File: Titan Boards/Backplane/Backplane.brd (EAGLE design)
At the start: 209.6 x 76.2 mm, 20 parts

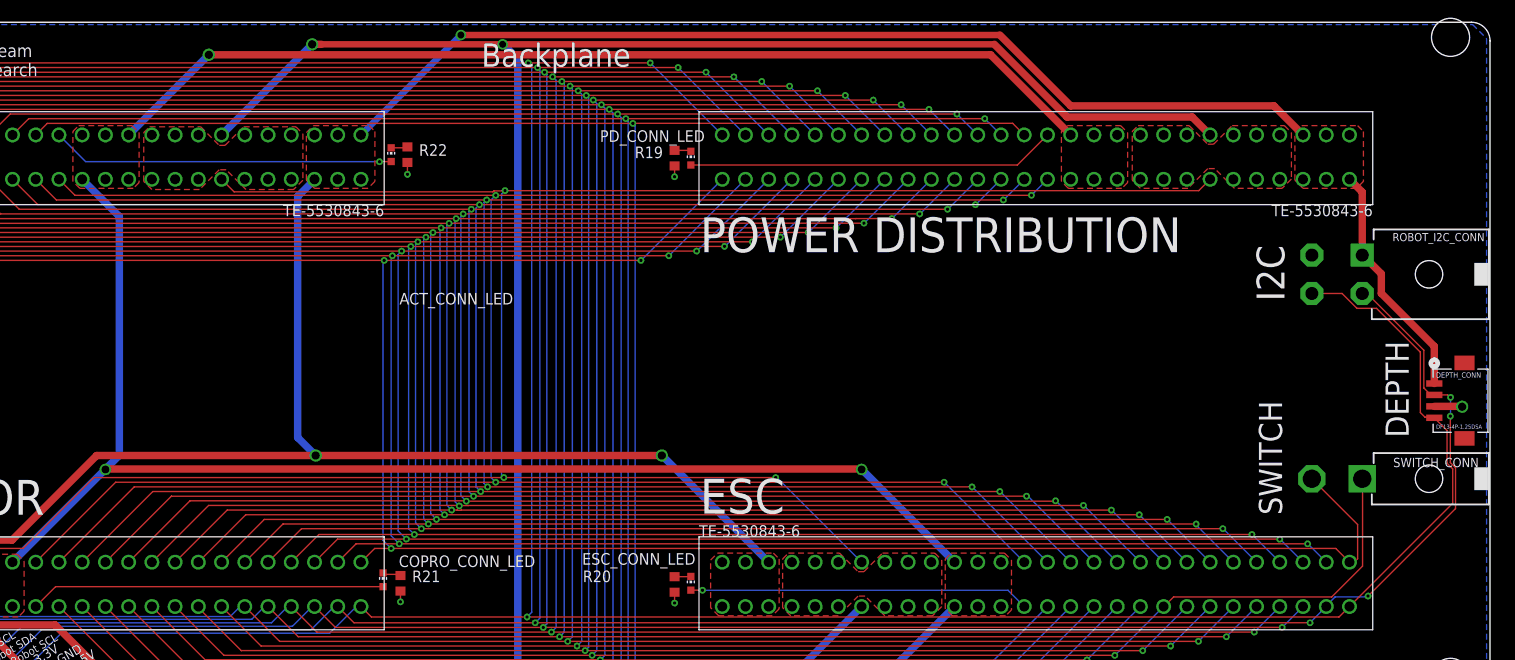
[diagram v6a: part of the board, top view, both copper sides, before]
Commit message: Backplane initial design review changes
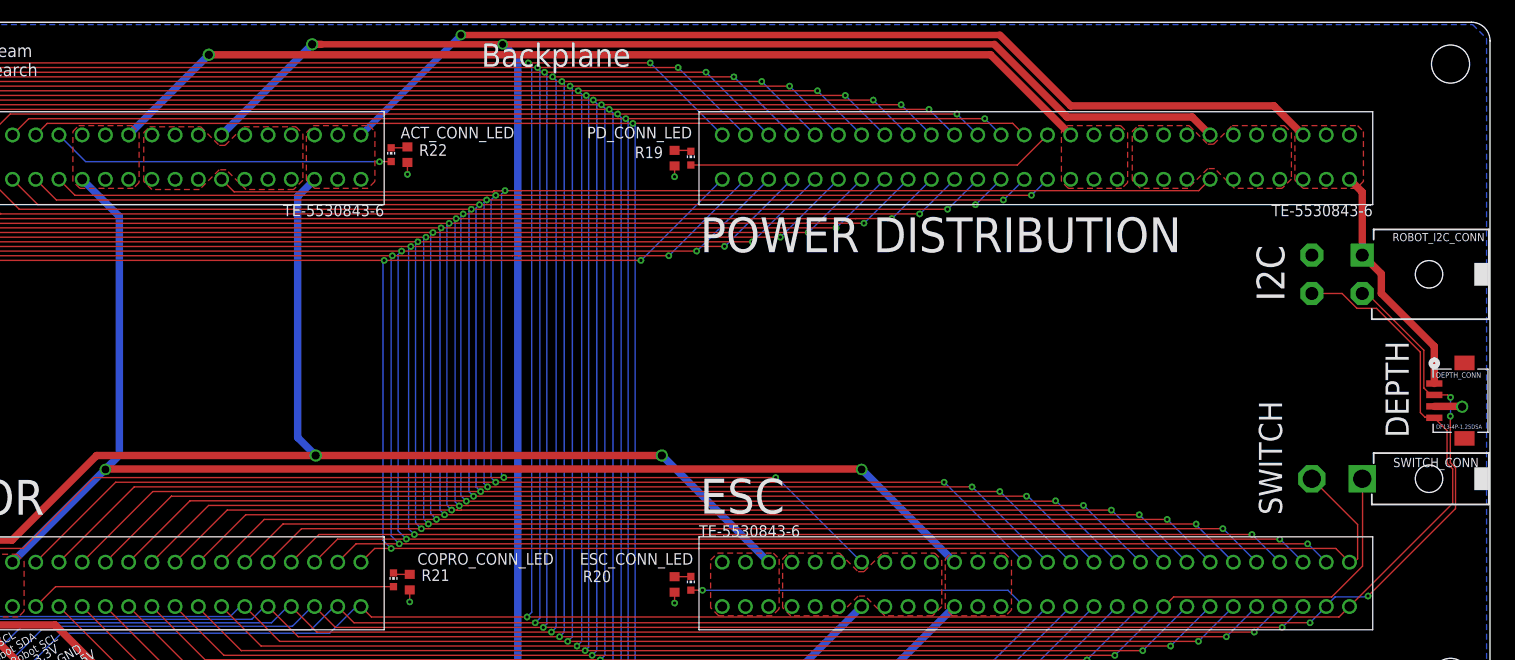
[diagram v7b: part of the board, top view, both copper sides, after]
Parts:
- moved COPRO_CONN_LED 1.14 mm to (89.7, 15.2)
- moved R21 1.02 mm to (91.4, 15.0)
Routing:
- net COPRO_CONN: track 38.9 -> 40.0 mm

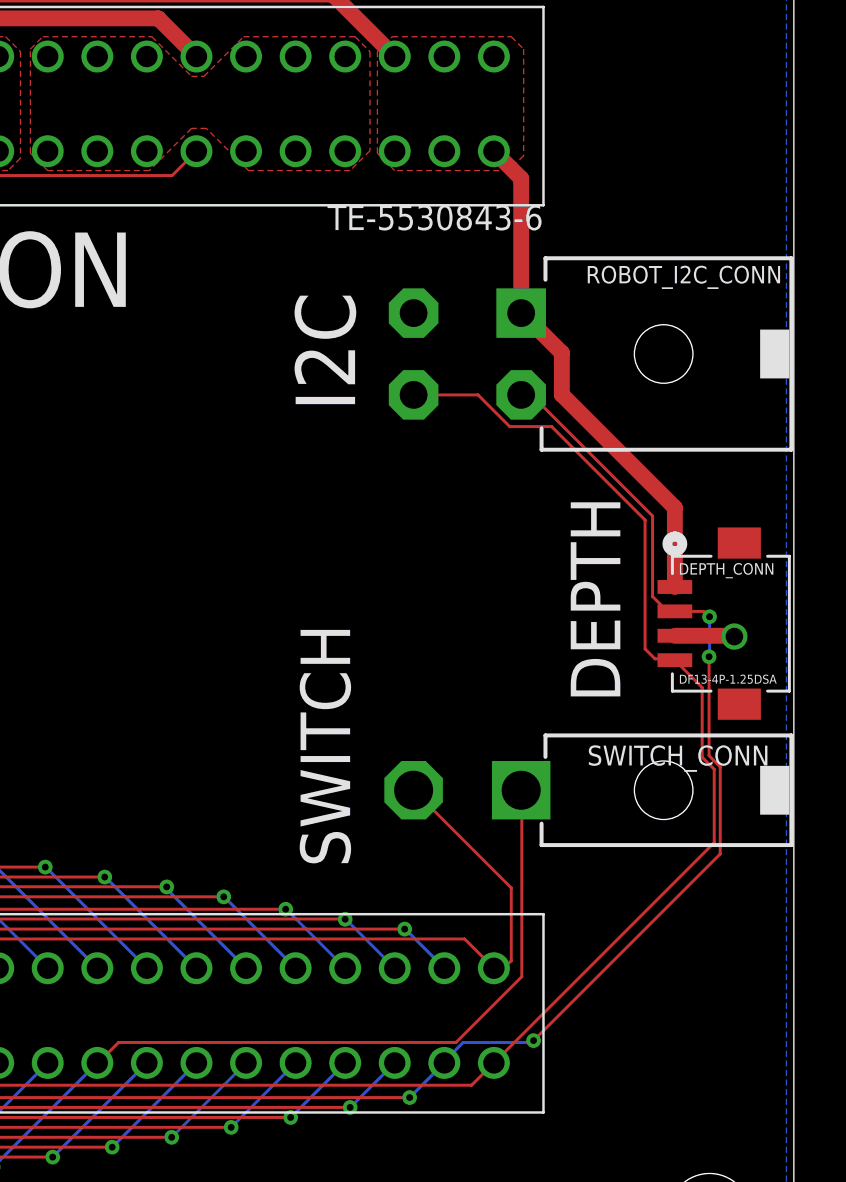
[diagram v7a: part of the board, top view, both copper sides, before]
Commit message: Backplane design review changes
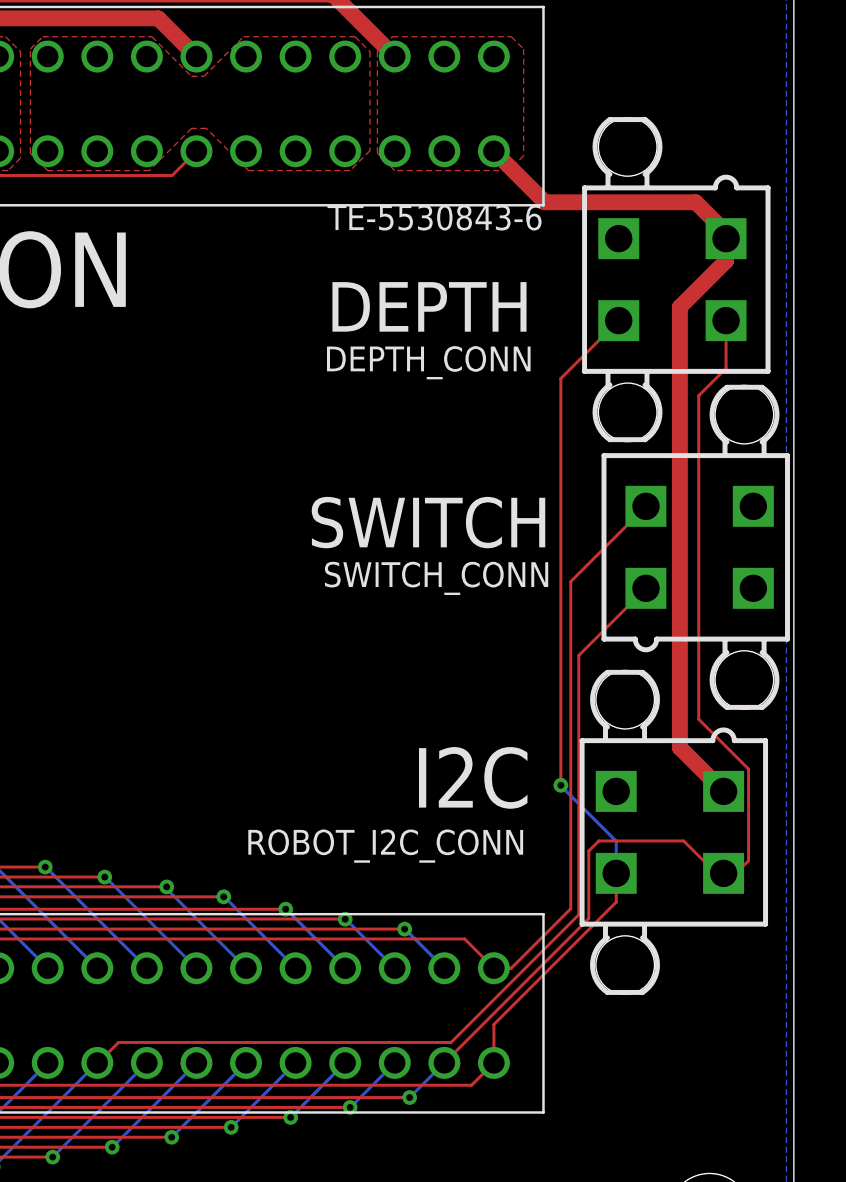
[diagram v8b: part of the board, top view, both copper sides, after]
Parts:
- DEPTH_CONN: value DF13-4P-1.25DSA -> (none); device DF13-4P-125DSA_Connector:CON4_1X4_U_DF13 -> con-molex-2:5566-4
- ROBOT_I2C_CONN: value 39-30-04?_S -> (none); device con-molex-mini-fit:39-30-?04? -> con-molex-2:5566-4
- SWITCH_CONN: value 39-30-02?_S -> (none); device con-molex-mini-fit:39-30-?02? -> con-molex-2:5566-4
- moved ROBOT_I2C_CONN 25.7 mm to (203.2, 24.1)
- moved DEPTH_CONN 15.7 mm to (203.3, 52.5)
- moved SWITCH_CONN 15.4 mm to (204.7, 38.7), turned to 270 degrees
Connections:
- net GND: now also SWITCH_CONN.3, SWITCH_CONN.4
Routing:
- net 3.3V: track 335.2 -> 353.2 mm
- net SPARE2: track 268.5 -> 284.1 mm
- net KILL_SWITCH: track 317.9 -> 330.8 mm
- net ROBOT_SCL: track 392.1 -> 386.1 mm, vias 3 -> 4
- net ROBOT_SDA: track 391.9 -> 396.8 mm, vias 8 -> 5
- net GND: track 8.05 -> 4.98 mm, vias 5 -> 4
